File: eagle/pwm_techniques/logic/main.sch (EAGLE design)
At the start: 72 parts, among them IC1 7805T, U2 TLE2426ID, U3 LM358ADT, U4 TL494CD, U5 SN74HC04D, U6 TL494CD

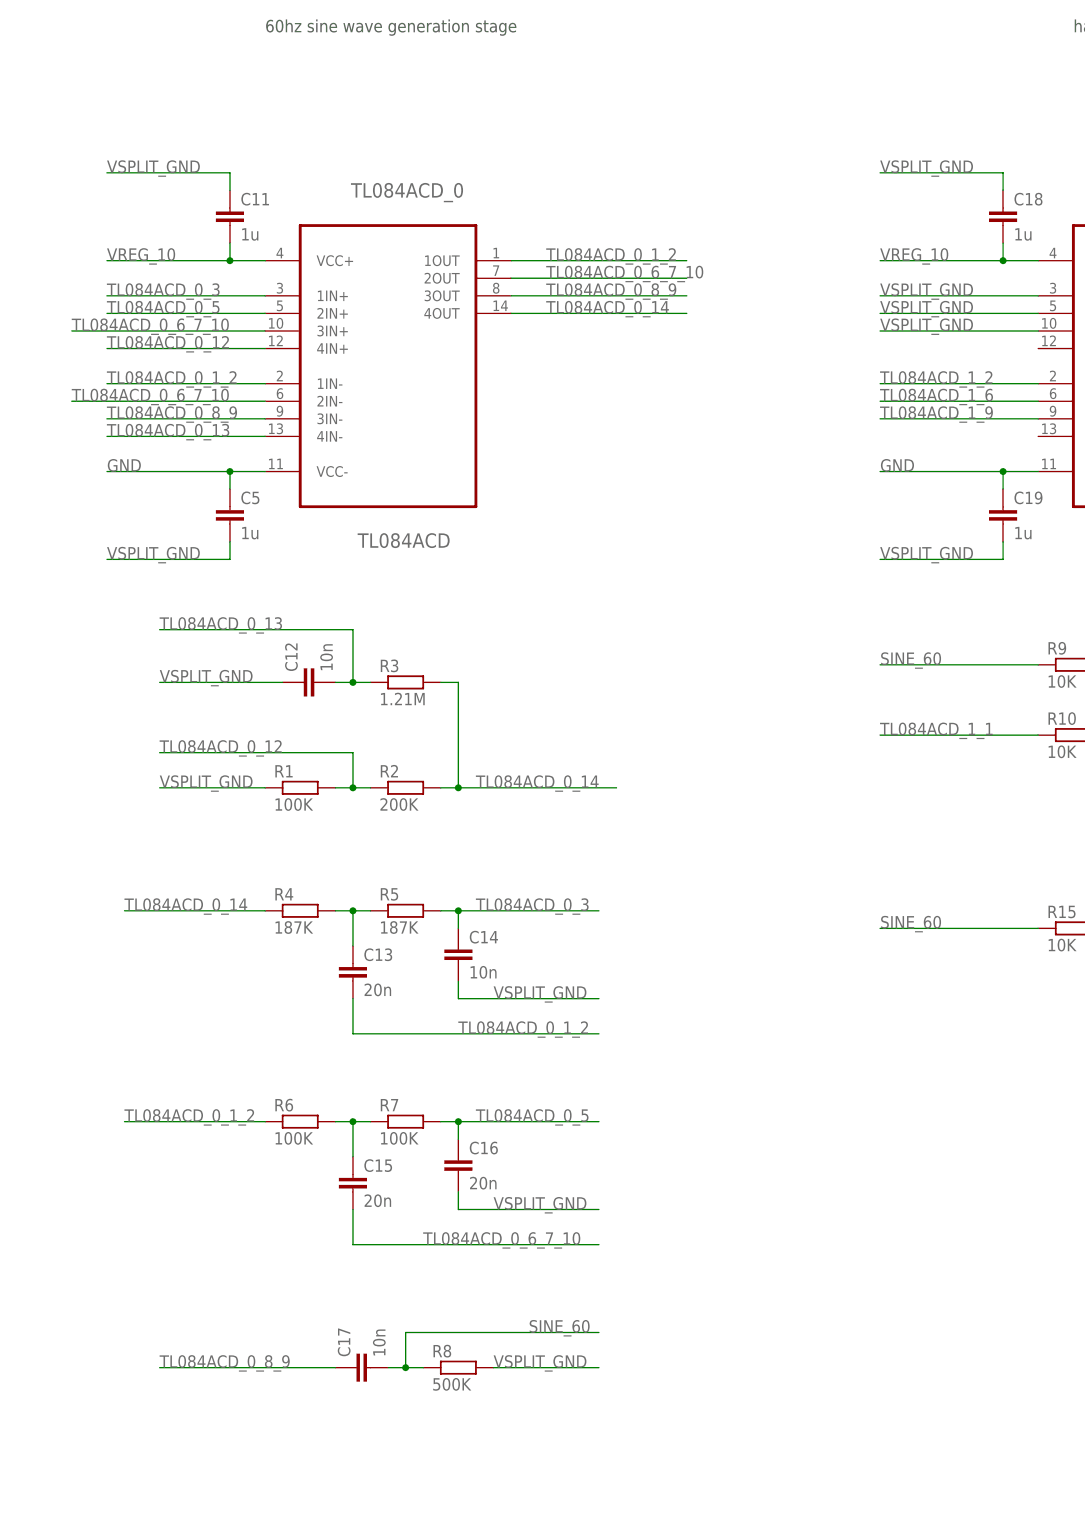
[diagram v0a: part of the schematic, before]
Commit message: [ update ] logic: 50hz, tunable sine wave
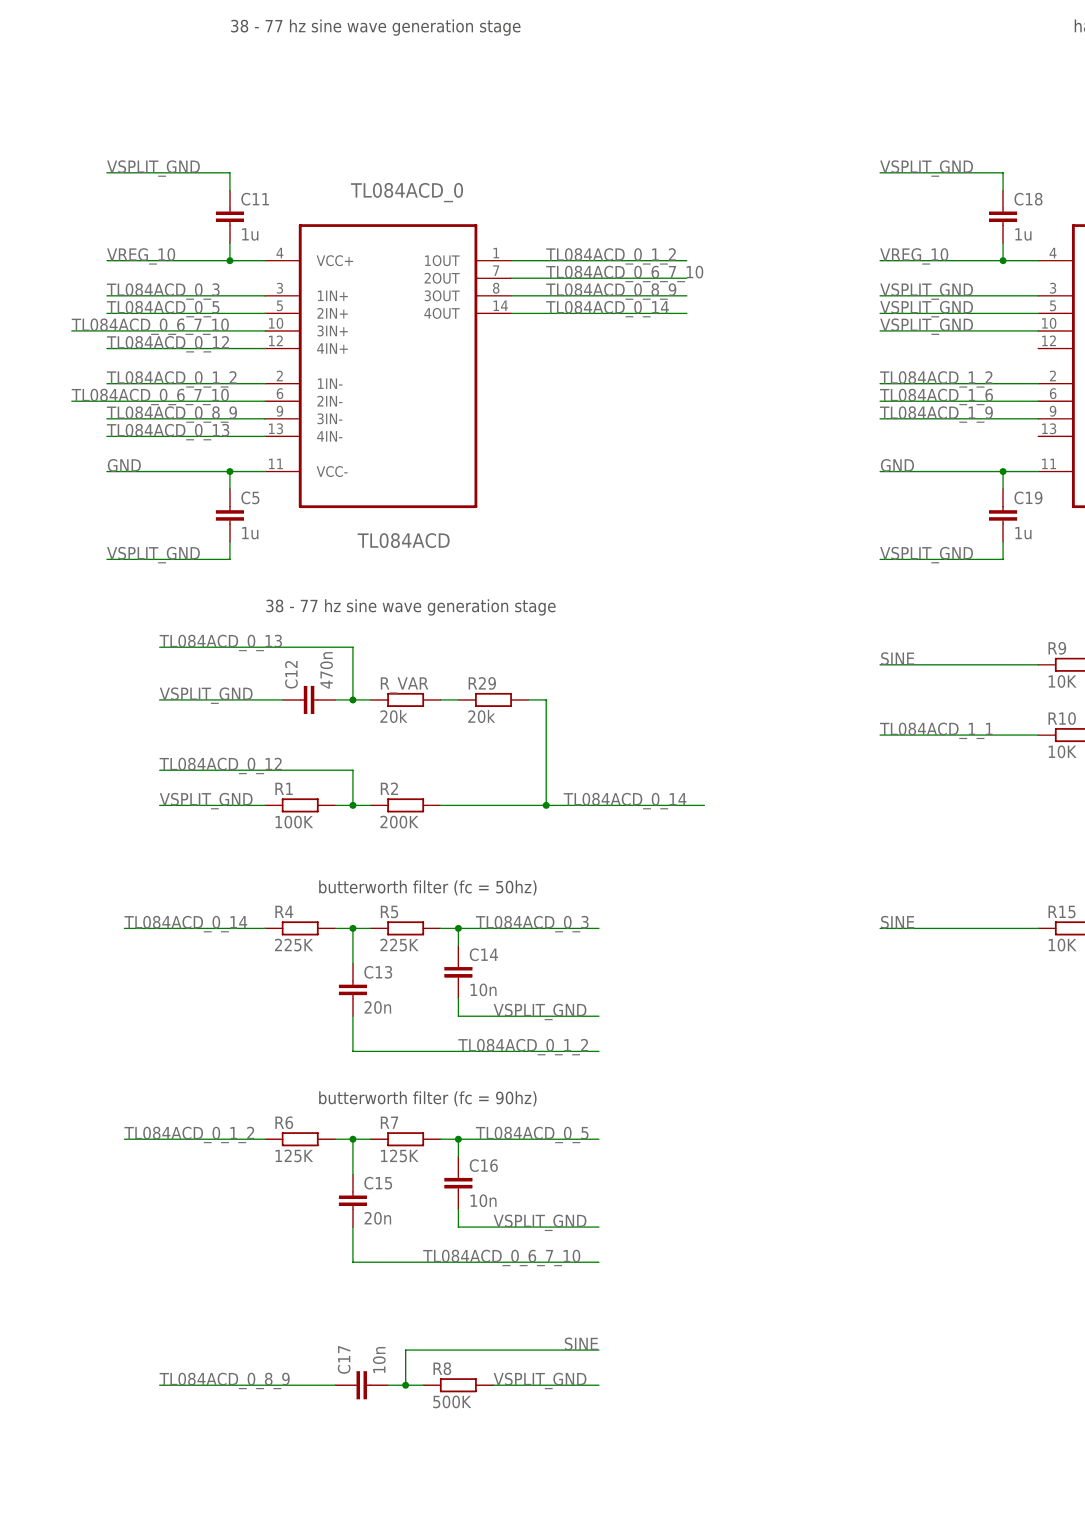
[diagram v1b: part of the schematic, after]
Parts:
- removed R3: 1.21M, resistor:R-EU_M1206
- added R29, R_VAR: 20k, resistor:R-EU_M1206
- C12: value 10n -> 470n
- C16: value 20n -> 10n
- R4, R5: value 187K -> 225K
- R6, R7: value 100K -> 125K
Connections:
- net SINE_60 renamed SINE
- new net N$10: R29.1, R_VAR.2
- net TL084ACD_0_13: now also R_VAR.1; no longer R3.1
- net TL084ACD_0_14: now also R29.2; no longer R3.2
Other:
- note added: "38 - 77 hz sine wave generation stage"
- note added: "butterworth filter (fc = 50hz)"
- note added: "butterworth filter (fc = 90hz)"
- note removed: "60hz sine wave generation stage"
- moved on the sheet: C12, C13, C14, C15, C16, C17, R1, R2, R4, R5, R6, R7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

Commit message: [ add ] ltspice/logic
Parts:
- R8: value 500K -> 625K
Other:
- note added: "38 - 77 hz square wave generation stage"
- note added: "high pass filter (fc = 25hz)"
- note added: "if R_VAR = 10.7K, freq = 50 hz"
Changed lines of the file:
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@@
 <part name="C16" library="rcl" deviceset="C-EU" device="C1206" value="10n"/>
 <part name="C17" library="rcl" deviceset="C-EU" device="C1206" value="10n"/>
-<part name="R8" library="resistor" deviceset="R-EU_" device="M1206" value="500K"/>
+<part name="R8" library="resistor" deviceset="R-EU_" device="M1206" value="625K"/>
 <part name="TL084ACD_1" library="tl084acd" deviceset="TL084ACD" device=""/>
 <part name="C18" library="rcl" deviceset="C-EU" device="C1206" value="1u"/>
@@
 <text x="-60.96" y="101.6" size="1.778" layer="97">battery connector</text>
 <text x="551.18" y="101.6" size="1.778" layer="97">output connector</text>
-<text x="111.76" y="17.78" size="1.778" layer="97">38 - 77 hz sine wave generation stage</text>
+<text x="111.76" y="20.32" size="1.778" layer="97">38 - 77 hz square wave generation stage</text>
 <text x="119.38" y="-22.86" size="1.778" layer="97">butterworth filter (fc = 50hz)</text>
 <text x="119.38" y="-53.34" size="1.778" layer="97">butterworth filter (fc = 90hz)</text>
+<text x="111.76" y="17.78" size="1.778" layer="97">if R_VAR = 10.7K, freq = 50 hz</text>
+<text x="119.38" y="-86.36" size="1.778" layer="97">high pass filter (fc = 25hz)</text>
 </plain>
 <instances>

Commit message: [ update, add ] ltspice/logic. add lm358, tl084 models
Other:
- note added: "butterworth lowpass filter (fc = 50hz)"
- note added: "butterworth lowpass filter (fc = 90hz)"
- note added: "outputs the rectified waveforms"
- note removed: "butterworth filter (fc = 50hz)"
- note removed: "butterworth filter (fc = 90hz)"
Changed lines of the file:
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@@
 <text x="551.18" y="101.6" size="1.778" layer="97">output connector</text>
 <text x="111.76" y="20.32" size="1.778" layer="97">38 - 77 hz square wave generation stage</text>
-<text x="119.38" y="-22.86" size="1.778" layer="97">butterworth filter (fc = 50hz)</text>
-<text x="119.38" y="-53.34" size="1.778" layer="97">butterworth filter (fc = 90hz)</text>
+<text x="119.38" y="-22.86" size="1.778" layer="97">butterworth lowpass filter (fc = 50hz)</text>
+<text x="119.38" y="-53.34" size="1.778" layer="97">butterworth lowpass filter (fc = 90hz)</text>
 <text x="111.76" y="17.78" size="1.778" layer="97">if R_VAR = 10.7K, freq = 50 hz</text>
 <text x="119.38" y="-86.36" size="1.778" layer="97">high pass filter (fc = 25hz)</text>
+<text x="228.6" y="99.06" size="1.778" layer="97">outputs the rectified waveforms</text>
 </plain>
 <instances>
